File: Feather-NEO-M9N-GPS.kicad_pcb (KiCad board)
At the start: 2 copper layers, 50.8 x 22.9 mm, 51 parts, among them IC1 PRTR5V0U2F,115, J6 USB_B_Micro, U1 NEO-M9N, U2 AP2112K-3.3

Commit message: Rev2.1 of NEO-M9N
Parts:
- ANT1: footprint SamacSys_Parts:UFLRSMT10 -> Feather-NEO-M9N-GPS:UFLRSMT10
- D4, D5: footprint SamacSys_Parts:SOD2513X110N -> Feather-NEO-M9N-GPS:SOD2513X110N
- IC1: footprint SamacSys_Parts:74LVC1G27GM115 -> Feather-NEO-M9N-GPS:74LVC1G27GM115
- U1: footprint RF_GPS:ublox_NEO -> Feather-NEO-M9N-GPS:NEO-M9N
- moved R3 1.25 mm to (169.5, 90.2)
- moved R4 1.15 mm to (168.0, 90.2)
- moved JP8 1.00 mm to (170.1, 93.3)
- moved JP9 1.00 mm to (167.8, 93.3)
- moved R11 0.69 mm to (170.2, 79.4)
- moved R10 0.39 mm to (170.2, 78.0)
- moved R14 0.32 mm to (150.9, 79.8)
- moved C4 0.13 mm to (150.1, 85.2)
- moved D3 0.08 mm to (139.7, 81.6)
- moved JP2 0.08 mm to (145.4, 81.6)
- moved R13 0.08 mm to (142.5, 81.6)
- turned U1 to 180 degrees
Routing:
- net GND: track 127.7 -> 172.9 mm, vias 141 -> 192
- net Net-(R4-Pad2): track 8.47 -> 10.1 mm
- net /SDA: track 9.43 -> 10.5 mm
- net +3V3: track 91.0 -> 91.8 mm
- net Net-(JP9-Pad2): track 1.54 -> 2.36 mm
- net Net-(JP3-Pad3): track 3.14 -> 2.35 mm
- net /INT: track 26.3 -> 27.0 mm
- net Net-(JP3-Pad1): track 3.07 -> 2.43 mm
- net /SCL: track 9.02 -> 8.38 mm
- net Net-(JP8-Pad1): track 1.76 -> 2.36 mm
- net Net-(JP6-Pad2): track 4.03 -> 4.60 mm
- net Net-(JP7-Pad2): track 2.14 -> 2.70 mm
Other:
- board text added: "Rev2.1 ABW 1/22/20"
- board text removed: "Rev2 ABW 1/6/20"

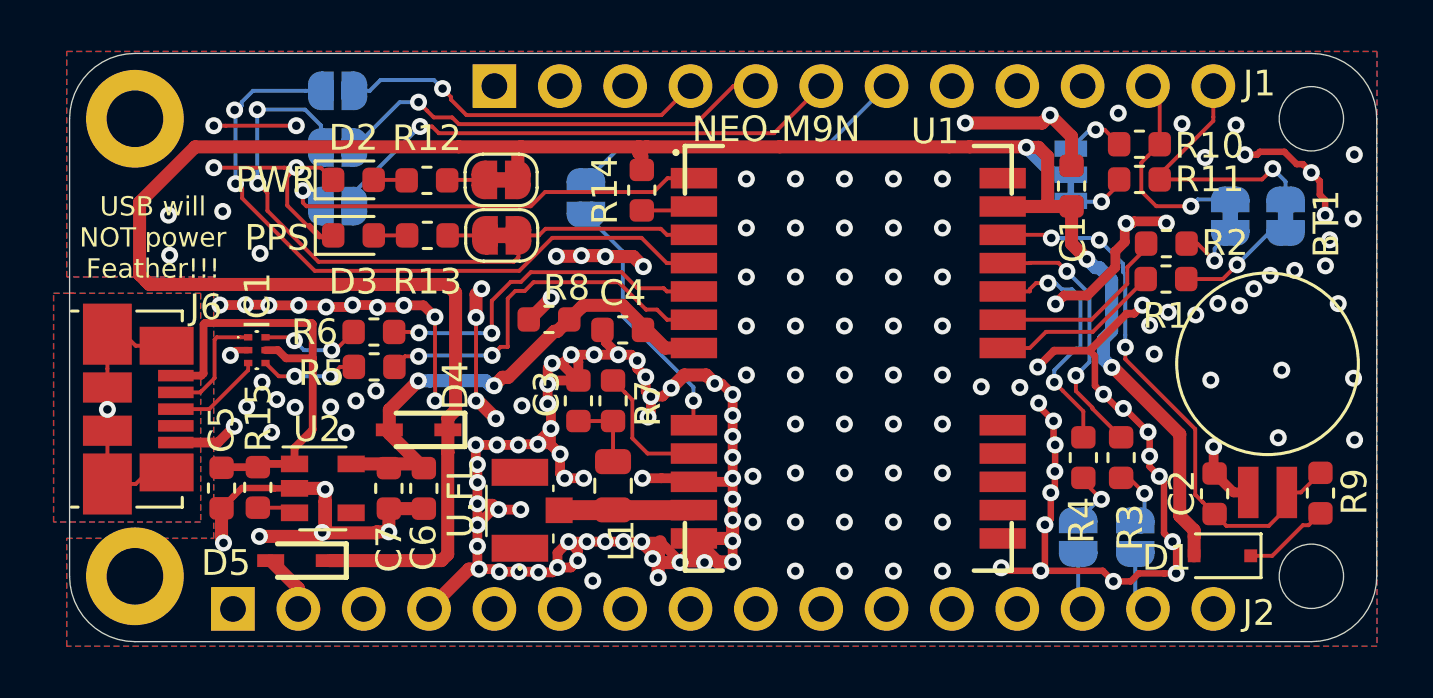
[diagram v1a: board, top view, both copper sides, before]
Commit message: Rev 2.2 designed
Lots of great feedback from the u-blox team. Hopefully this revision fixes a lot of the problems they pointed out
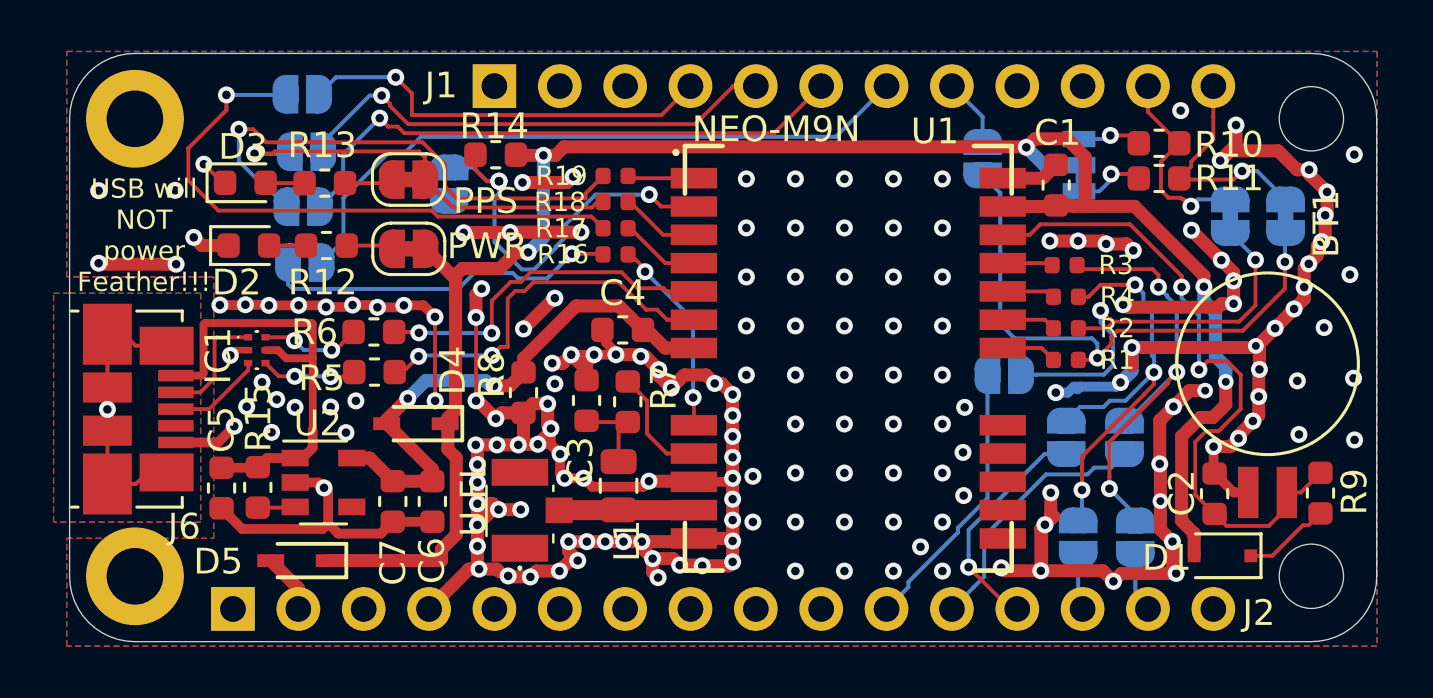
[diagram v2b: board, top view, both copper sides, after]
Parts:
- added JP13: MISO, Jumper:SolderJumper-2_P1.3mm_Open_RoundedPad1.0x1.5mm, B.Cu at (167.4, 89.4)
- added JP14: MOSI, Jumper:SolderJumper-2_P1.3mm_Open_RoundedPad1.0x1.5mm, B.Cu at (169.6, 89.4)
- added JP15: SCK, Jumper:SolderJumper-2_P1.3mm_Open_RoundedPad1.0x1.5mm, B.Cu at (165.0, 87.0)
- added JP16: ~CS, Jumper:SolderJumper-2_P1.3mm_Open_RoundedPad1.0x1.5mm, B.Cu at (164.1, 78.6)
- added JP4: SPI, Jumper:SolderJumper-2_P1.3mm_Open_RoundedPad1.0x1.5mm, B.Cu at (143.4, 79.6)
- added R16: 33, Resistor_SMD:R_0402_1005Metric, F.Cu at (149.9, 82.3)
- added R17: 33, Resistor_SMD:R_0402_1005Metric, F.Cu at (149.9, 81.3)
- added R18: 33, Resistor_SMD:R_0402_1005Metric, F.Cu at (149.9, 80.3)
- added R19: 33, Resistor_SMD:R_0402_1005Metric, F.Cu at (149.9, 79.3)
- JP5: value ~RESET_GPS -> ~RST GPS
- R1, R2, R3, R4: footprint Resistor_SMD:R_0603_1608Metric -> Resistor_SMD:R_0402_1005Metric
- moved JP5 11.2 mm to (137.8, 82.6), turned to 0 degrees
- moved R3 7.79 mm to (167.3, 82.7), turned to 180 degrees
- moved R4 6.29 mm to (167.4, 84.0), turned to 180 degrees
- moved R14 5.84 mm to (145.2, 78.4), turned to 0 degrees
- moved R2 5.11 mm to (167.4, 85.2)
- moved R1 5.00 mm to (167.4, 86.4)
- moved D2 4.80 mm to (135.6, 82.0)
- moved D3 4.67 mm to (135.5, 79.5)
- moved R12 4.65 mm to (138.6, 82.0)
- moved JP1 4.48 mm to (141.8, 82.1)
- moved R13 4.47 mm to (138.6, 79.5)
- moved JP2 4.22 mm to (141.8, 79.4)
- moved R8 3.01 mm to (146.3, 87.7), turned to 90 degrees
- moved JP10 1.38 mm to (137.7, 76.1)
- moved JP12 1.34 mm to (137.7, 80.5)
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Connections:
- J2 pad 11: Net-(J2-Pad11) -> /SCK
- J2 pad 12: Net-(J2-Pad12) -> /MOSI
- J2 pad 13: Net-(J2-Pad13) -> /MISO
- JP6 pad 1: /SDA -> Net-(JP16-Pad2)
- JP6 pad 2: Net-(JP6-Pad2) -> /SDA
- JP7 pad 1: /SCL -> Net-(JP15-Pad2)
- JP7 pad 2: Net-(JP7-Pad2) -> /SCL
- R1 pad 1: Net-(JP6-Pad2) -> Net-(JP16-Pad2)
- R2 pad 1: Net-(JP7-Pad2) -> Net-(JP15-Pad2)
- U1 pad 1: /~SAFE -> Net-(R19-Pad2)
- U1 pad 3: /PPS -> Net-(R18-Pad2)
- U1 pad 4: /INT -> Net-(R17-Pad2)
- U1 pad 8: /~RESET_GPS -> Net-(R16-Pad2)
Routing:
- net Net-(JP16-Pad2): track 0.00 -> 22.9 mm, vias 0 -> 2
- net +3V3: track 91.8 -> 73.3 mm, vias 3 -> 5
- net Net-(JP15-Pad2): track 0.00 -> 17.5 mm, vias 0 -> 2
- net Net-(JP14-Pad1): track 2.36 -> 18.0 mm, vias 1 -> 3
- net Net-(JP13-Pad2): track 2.36 -> 17.4 mm, vias 1 -> 3
- net /D_SEL: track 2.09 -> 16.2 mm, vias 0 -> 3
- net /10`: track 13.2 -> 25.8 mm
- net GND: track 172.9 -> 184.8 mm, vias 192 -> 181
- net /SCK: track 0.00 -> 10.7 mm
- net /MOSI: track 0.00 -> 10.1 mm
- net /PPS: track 26.3 -> 16.5 mm, vias 2 -> 1
- net /MISO: track 0.00 -> 9.03 mm, vias 0 -> 1
- net Net-(R3-Pad2): track 10.4 -> 1.96 mm, vias 2 -> 0
- net Net-(R4-Pad2): track 10.1 -> 2.08 mm, vias 2 -> 0
- net Net-(R16-Pad2): track 0.00 -> 7.70 mm, vias 0 -> 2
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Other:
- board text added: "0x42"
- board text added: "9"
- board text added: "Rev2.2 ABW 1/31/20"
- board text removed: "Address: 0x42"
- board text removed: "Rev2.1 ABW 1/22/20"

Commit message: Rev 2.3, u-blox approved!
Rev 2.3 is finished! It has been approved by the design team at u-blox. Next step is to see if Adafruit would be interested in my continuing this design and possibly getting it onto their store if it works well enough
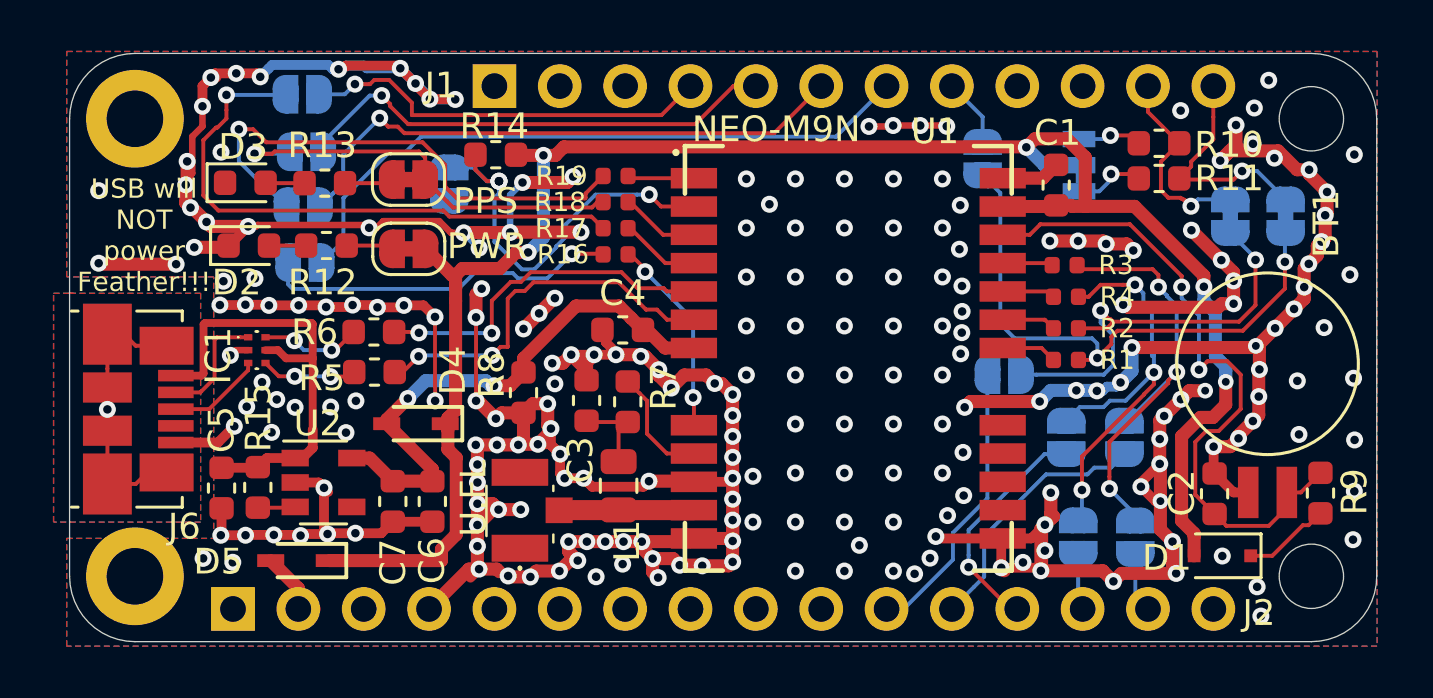
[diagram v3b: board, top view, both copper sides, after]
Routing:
- net GND: track 184.8 -> 237.1 mm, vias 181 -> 238
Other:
- board text added: "Rev2.3 ABW 2/24/20"
- board text removed: "Rev2.2 ABW 1/31/20"
- board text removed: "UART"
